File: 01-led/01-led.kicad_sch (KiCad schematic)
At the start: 4 parts, among them J1 Conn_01x02_Socket, J2 Conn_01x02_Socket

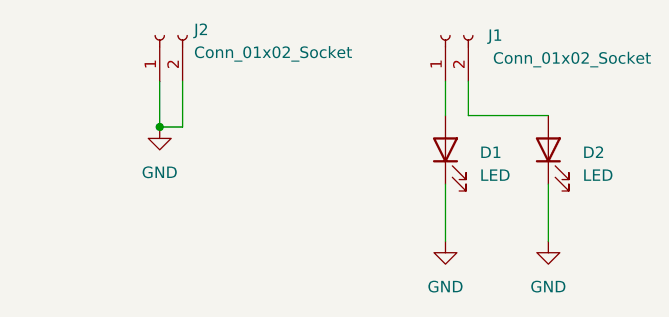
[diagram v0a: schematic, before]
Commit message: 01-led: update schematics and pcb
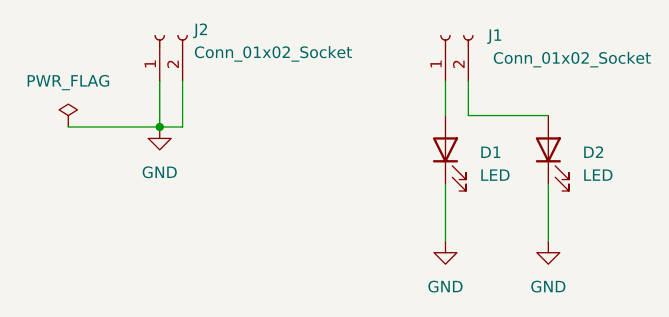
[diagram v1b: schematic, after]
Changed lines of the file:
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@@
+    (stroke (width 0) (type default))
+  )
+  (wire (pts (xy 77.47 67.31) (xy 87.63 67.31))
     (stroke (width 0) (type default))
   )
@@
         )
       )
+    )
+  )
+  (symbol (lib_id "power:PWR_FLAG") (at 77.47 67.31 0) (unit 1)
+    (in_bom yes) (on_board yes) (dnp no) (fields_autoplaced)
+    (property "Reference" "#FLG01" (at 77.47 65.405 0)
+      (effects (font (size 1.27 1.27)) hide)
+    )
+    (property "Value" "PWR_FLAG" (at 77.47 62.23 0)
+      (effects (font (size 1.27 1.27)))
+    )
+    (property "Footprint" "" (at 77.47 67.31 0)
+      (effects (font (size 1.27 1.27)) hide)
+    )
+    (property "Datasheet" "~" (at 77.47 67.31 0)
+      (effects (font (size 1.27 1.27)) hide)
+    )
+    (pin "1")
+    (instances
+      (project "01-led"
+        (path "/d7cbc107-4721-4d28-9271-a3fbf995a958"
+          (reference "#FLG01") (unit 1)
+        )
+      )

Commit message: update schematics
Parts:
- D1, D2: footprint LED_THT:LED_D3.0mm -> Library:LED_THT__LED_D3.0mm
- J1, J2: footprint Connector_PinSocket_2.54mm:PinSocket_1x02_P2.54mm_Vertical -> Library:Connector__PinSocket_1x02_P2.54mm_Vertical
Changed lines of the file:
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@@
       (effects (font (size 1.27 1.27)) (justify left))
     )
-    (property "Footprint" "Connector_PinSocket_2.54mm:PinSocket_1x02_P2.54mm_Vertical" (at 119.38 57.15 0)
+    (property "Footprint" "Library:Connector__PinSocket_1x02_P2.54mm_Vertical" (at 119.38 57.15 0)
       (effects (font (size 1.27 1.27)) hide)
     )
@@
       (effects (font (size 1.27 1.27)) (justify right))
     )
-    (property "Footprint" "LED_THT:LED_D3.0mm" (at 119.38 69.85 0)
+    (property "Footprint" "Library:LED_THT__LED_D3.0mm" (at 119.38 69.85 0)
       (effects (font (size 1.27 1.27)) hide)
     )
@@
       (effects (font (size 1.27 1.27)) (justify right))
     )
-    (property "Footprint" "Connector_PinSocket_2.54mm:PinSocket_1x02_P2.54mm_Vertical" (at 87.63 57.15 0)
+    (property "Footprint" "Library:Connector__PinSocket_1x02_P2.54mm_Vertical" (at 87.63 57.15 0)
       (effects (font (size 1.27 1.27)) hide)
     )
@@
       (effects (font (size 1.27 1.27)) (justify right))
     )
-    (property "Footprint" "LED_THT:LED_D3.0mm" (at 130.81 69.85 0)
+    (property "Footprint" "Library:LED_THT__LED_D3.0mm" (at 130.81 69.85 0)
       (effects (font (size 1.27 1.27)) hide)
     )

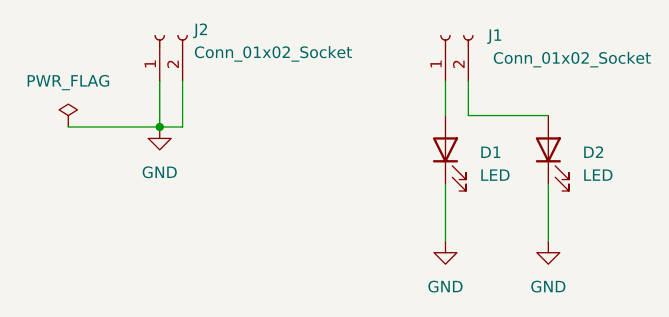
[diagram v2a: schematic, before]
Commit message: led: change references (D0)
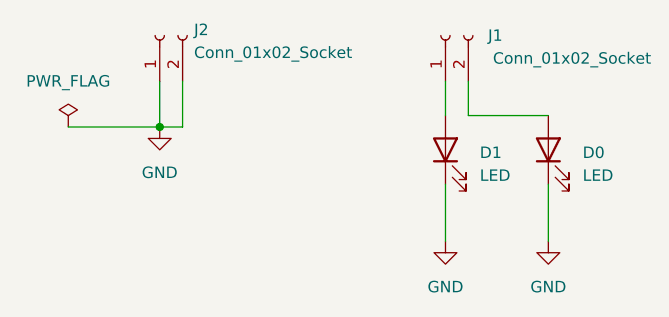
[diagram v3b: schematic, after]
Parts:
- renumbered D2 to D0
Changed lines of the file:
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@@
   (symbol (lib_id "Device:LED") (at 130.81 69.85 90) (unit 1)
     (in_bom yes) (on_board yes) (dnp no) (fields_autoplaced)
-    (property "Reference" "D2" (at 134.62 70.1675 90)
+    (property "Reference" "D0" (at 134.62 70.1675 90)
       (effects (font (size 1.27 1.27)) (justify right))
     )
@@
       (project "01-led"
         (path "/d7cbc107-4721-4d28-9271-a3fbf995a958"
-          (reference "D2") (unit 1)
+          (reference "D0") (unit 1)
         )
       )
